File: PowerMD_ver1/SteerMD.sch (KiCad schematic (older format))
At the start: 228 parts, among them P1 SWD, P10 OUT_1, P11 ENC_0, P13 ENC_1, P14 I/O_1, P15 OUT_0, P2 MOTOR_COOLING, P3 CAN, P4 CAN, P5 SERIAL, P6 I/O_0, P7 FAN, P8 BATT_IN, P9 BATT_IN, Q1 MOSFET_N, Q2 MOSFET_N, Q3 MOSFET_N, Q4 MOSFET_N, Q5 MOSFET_N, Q6 MOSFET_N, Q7 MOSFET_N, Q8 MOSFET_N, SW1 RST, SW3 SW0, SW4 SW1, U1 MAX3051, U10 ACS758, U11 POWER_ON, U12 SI8274, U13 ACS758, U14 SI8274, U15 AZ1086H, U16 LOGO, U17 AQM0802, U18 LTC2644, U19 ADRESS, U2 BD9G101, U3 STM32F405RG, U4 SI8274, U5 SI8900, U6 ADC_~RST, U7 BD9G101G, U8 SI8274, U9 BD33FA1, Y1 8MHz

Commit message: だいぶ良いところまで進んだ
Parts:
- added C66, C67: 0.1u, Mizz_lib:1608_WP, symbol SteerMD-rescue:C-Device-MD_Enbarr_x2-rescue-F4_CAN_DCMD-rescue
- C65: footprint Capacitor_SMD:C_0603_1608Metric -> Mizz_lib:1608_WP
- D1, D10, D11, D12, D13, D14, D17, D19, D2, D20, D3, D6: footprint Mizz_lib:1608_WP -> Diode_SMD:D_SOD-123
- R19, R20, R28, R29, R55, R56, R58, R59: value 1 -> 10
- R40: value 4.7k -> 20k
- R75, R76, R77, R78: footprint Resistor_SMD:R_0603_1608Metric -> Mizz_lib:1608_WP
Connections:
- net GNDPWR: now also C66.2, C67.2
- net MOTOR0_OUT: now also C67.1
- net MOTOR1_OUT: now also C66.1
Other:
- moved on the sheet: D12, D17, R77, R78
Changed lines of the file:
@@
 P 8850 3625
 F 0 "R40" H 8920 3671 50  0000 L CNN
-F 1 "4.7k" H 8920 3580 50  0000 L CNN
+F 1 "20k" H 8920 3580 50  0000 L CNN
 F 2 "Resistor_SMD:R_0603_1608Metric" V 8780 3625 50  0001 C CNN
 F 3 "~" H 8850 3625 50  0001 C CNN
@@
 P 13425 8600
 F 0 "R59" V 13218 8600 50  0000 C CNN
-F 1 "1" V 13309 8600 50  0000 C CNN
+F 1 "10" V 13309 8600 50  0000 C CNN
 F 2 "Mizz_lib:1608_WP" V 13355 8600 50  0001 C CNN
 F 3 "~" H 13425 8600 50  0001 C CNN
@@
 F 0 "D11" H 13775 8408 40  0000 C CNN
 F 1 "DIODE" H 13775 8484 40  0000 C CNN
-F 2 "Mizz_lib:1608_WP" H 13775 8600 60  0001 C CNN
+F 2 "Diode_SMD:D_SOD-123" H 13775 8600 60  0001 C CNN
 F 3 "" H 13775 8600 60  0000 C CNN
 	1    13775 8600
@@
 P 13425 7850
 F 0 "R58" V 13218 7850 50  0000 C CNN
-F 1 "1" V 13309 7850 50  0000 C CNN
+F 1 "10" V 13309 7850 50  0000 C CNN
 F 2 "Mizz_lib:1608_WP" V 13355 7850 50  0001 C CNN
 F 3 "~" H 13425 7850 50  0001 C CNN
@@
 F 0 "D3" H 13775 7658 40  0000 C CNN
 F 1 "DIODE" H 13775 7734 40  0000 C CNN
-F 2 "Mizz_lib:1608_WP" H 13775 7850 60  0001 C CNN
+F 2 "Diode_SMD:D_SOD-123" H 13775 7850 60  0001 C CNN
 F 3 "" H 13775 7850 60  0000 C CNN
 	1    13775 7850
@@
 P 11475 8600
 F 0 "R56" V 11268 8600 50  0000 C CNN
-F 1 "1" V 11359 8600 50  0000 C CNN
+F 1 "10" V 11359 8600 50  0000 C CNN
 F 2 "Mizz_lib:1608_WP" V 11405 8600 50  0001 C CNN
 F 3 "~" H 11475 8600 50  0001 C CNN
@@
 F 0 "D2" H 11125 8408 40  0000 C CNN
 F 1 "DIODE" H 11125 8484 40  0000 C CNN
-F 2 "Mizz_lib:1608_WP" H 11125 8600 60  0001 C CNN
+F 2 "Diode_SMD:D_SOD-123" H 11125 8600 60  0001 C CNN
 F 3 "" H 11125 8600 60  0000 C CNN
 	1    11125 8600
@@
 P 11475 7850
 F 0 "R55" V 11268 7850 50  0000 C CNN
-F 1 "1" V 11359 7850 50  0000 C CNN
+F 1 "10" V 11359 7850 50  0000 C CNN
 F 2 "Mizz_lib:1608_WP" V 11405 7850 50  0001 C CNN
 F 3 "~" H 11475 7850 50  0001 C CNN
@@
 F 0 "D1" H 11125 7658 40  0000 C CNN
 F 1 "DIODE" H 11125 7734 40  0000 C CNN
-F 2 "Mizz_lib:1608_WP" H 11125 7850 60  0001 C CNN
+F 2 "Diode_SMD:D_SOD-123" H 11125 7850 60  0001 C CNN
 F 3 "" H 11125 7850 60  0000 C CNN
 	1    11125 7850
@@
 P 13425 5775
 F 0 "R29" V 13218 5775 50  0000 C CNN
-F 1 "1" V 13309 5775 50  0000 C CNN
+F 1 "10" V 13309 5775 50  0000 C CNN
 F 2 "Mizz_lib:1608_WP" V 13355 5775 50  0001 C CNN
 F 3 "~" H 13425 5775 50  0001 C CNN
@@
 F 0 "D20" H 13775 5583 40  0000 C CNN
 F 1 "DIODE" H 13775 5659 40  0000 C CNN
-F 2 "Mizz_lib:1608_WP" H 13775 5775 60  0001 C CNN
+F 2 "Diode_SMD:D_SOD-123" H 13775 5775 60  0001 C CNN
 F 3 "" H 13775 5775 60  0000 C CNN
 	1    13775 5775
@@
 P 13425 5025
 F 0 "R28" V 13218 5025 50  0000 C CNN
-F 1 "1" V 13309 5025 50  0000 C CNN
+F 1 "10" V 13309 5025 50  0000 C CNN
 F 2 "Mizz_lib:1608_WP" V 13355 5025 50  0001 C CNN
 F 3 "~" H 13425 5025 50  0001 C CNN
@@
 F 0 "D19" H 13775 4833 40  0000 C CNN
 F 1 "DIODE" H 13775 4909 40  0000 C CNN
-F 2 "Mizz_lib:1608_WP" H 13775 5025 60  0001 C CNN
+F 2 "Diode_SMD:D_SOD-123" H 13775 5025 60  0001 C CNN
 F 3 "" H 13775 5025 60  0000 C CNN
 	1    13775 5025
@@
 P 11475 5775
 F 0 "R20" V 11268 5775 50  0000 C CNN
-F 1 "1" V 11359 5775 50  0000 C CNN
+F 1 "10" V 11359 5775 50  0000 C CNN
 F 2 "Mizz_lib:1608_WP" V 11405 5775 50  0001 C CNN
 F 3 "~" H 11475 5775 50  0001 C CNN
@@
 F 0 "D14" H 11125 5583 40  0000 C CNN
 F 1 "DIODE" H 11125 5659 40  0000 C CNN
-F 2 "Mizz_lib:1608_WP" H 11125 5775 60  0001 C CNN
+F 2 "Diode_SMD:D_SOD-123" H 11125 5775 60  0001 C CNN
 F 3 "" H 11125 5775 60  0000 C CNN
 	1    11125 5775
@@
 P 11475 5025
 F 0 "R19" V 11268 5025 50  0000 C CNN
-F 1 "1" V 11359 5025 50  0000 C CNN
+F 1 "10" V 11359 5025 50  0000 C CNN
 F 2 "Mizz_lib:1608_WP" V 11405 5025 50  0001 C CNN
 F 3 "~" H 11475 5025 50  0001 C CNN
@@
 F 0 "D13" H 11125 4833 40  0000 C CNN
 F 1 "DIODE" H 11125 4909 40  0000 C CNN
-F 2 "Mizz_lib:1608_WP" H 11125 5025 60  0001 C CNN
+F 2 "Diode_SMD:D_SOD-123" H 11125 5025 60  0001 C CNN
 F 3 "" H 11125 5025 60  0000 C CNN
 	1    11125 5025
@@
 	1    0    0    -1
 $EndComp
-Text Label 14600 3375 0    50   ~ 0
+Text Label 14750 3375 0    50   ~ 0
 OUT0_L
-Text Label 14600 3475 0    50   ~ 0
+Text Label 14750 3475 0    50   ~ 0
 OUT0_R
 $Comp
 L SteerMD-rescue:DIODE-device-MD_Enbarr_x2-rescue-F4_CAN_DCMD-rescue D17
 U 1 1 5E77099F
-P 14400 3475
-F 0 "D17" H 14400 3283 40  0000 C CNN
-F 1 "DIODE" H 14400 3359 40  0000 C CNN
-F 2 "Mizz_lib:1608_WP" H 14400 3475 60  0001 C CNN
-F 3 "" H 14400 3475 60  0000 C CNN
-	1    14400 3475
+P 14550 3475
+F 0 "D17" H 14550 3283 40  0000 C CNN
+F 1 "DIODE" H 14550 3359 40  0000 C CNN
+F 2 "Diode_SMD:D_SOD-123" H 14550 3475 60  0001 C CNN
+F 3 "" H 14550 3475 60  0000 C CNN
+	1    14550 3475
 	-1   0    0    1
 $EndComp
@@
 L SteerMD-rescue:DIODE-device-MD_Enbarr_x2-rescue-F4_CAN_DCMD-rescue D12
 U 1 1 5E771A60
-P 14400 3375
-F 0 "D12" H 14400 3183 40  0000 C CNN
-F 1 "DIODE" H 14400 3259 40  0000 C CNN
-F 2 "Mizz_lib:1608_WP" H 14400 3375 60  0001 C CNN
-F 3 "" H 14400 3375 60  0000 C CNN
-	1    14400 3375
+P 14550 3375
+F 0 "D12" H 14550 3183 40  0000 C CNN
+F 1 "DIODE" H 14550 3259 40  0000 C CNN
+F 2 "Diode_SMD:D_SOD-123" H 14550 3375 60  0001 C CNN
+F 3 "" H 14550 3375 60  0000 C CNN
+	1    14550 3375
 	-1   0    0    1
 $EndComp
 Wire Wire Line
-	14200 3375 14200 3475
+	14350 3375 14350 3475
 $Comp
 L SteerMD-rescue:R-Device-MD_Enbarr_x2-rescue-F4_CAN_DCMD-rescue R77
 U 1 1 5E7BD65D
-P 14200 3625
-F 0 "R77" H 14270 3671 50  0000 L CNN
-F 1 "10k" H 14270 3580 50  0000 L CNN
-F 2 "Resistor_SMD:R_0603_1608Metric" V 14130 3625 50  0001 C CNN
-F 3 "~" H 14200 3625 50  0001 C CNN
-	1    14200 3625
+P 14350 3625
+F 0 "R77" H 14420 3671 50  0000 L CNN
+F 1 "10k" H 14420 3580 50  0000 L CNN
+F 2 "Mizz_lib:1608_WP" V 14280 3625 50  0001 C CNN
+F 3 "~" H 14350 3625 50  0001 C CNN
+	1    14350 3625
 	1    0    0    -1
 $EndComp
-Connection ~ 14200 3475
+Connection ~ 14350 3475
 $Comp
 L SteerMD-rescue:R-Device-MD_Enbarr_x2-rescue-F4_CAN_DCMD-rescue R78
 U 1 1 5E7BED02
-P 14200 3975
-F 0 "R78" H 14270 4021 50  0000 L CNN
-F 1 "1k" H 14270 3930 50  0000 L CNN
-F 2 "Resistor_SMD:R_0603_1608Metric" V 14130 3975 50  0001 C CNN
-F 3 "~" H 14200 3975 50  0001 C CNN
-	1    14200 3975
+P 14350 3975
+F 0 "R78" H 14420 4021 50  0000 L CNN
+F 1 "1k" H 14420 3930 50  0000 L CNN
+F 2 "Mizz_lib:1608_WP" V 14280 3975 50  0001 C CNN
+F 3 "~" H 14350 3975 50  0001 C CNN
+	1    14350 3975
 	1    0    0    -1
 $EndComp
-Text Label 14150 3800 2    50   ~ 0
+Text Label 14300 3800 2    50   ~ 0
 MOTOR0_OUT
 Wire Wire Line
-	14150 3800 14200 3800
+	14300 3800 14350 3800
 Wire Wire Line
-	14200 3800 14200 3775
+	14350 3800 14350 3775
 Wire Wire Line
-	14200 3800 14200 3825
-Connection ~ 14200 3800
+	14350 3800 14350 3825
+Connection ~ 14350 3800
 $Comp
 L SteerMD-rescue:GNDPWR-power-MD_Enbarr_x2-rescue-F4_CAN_DCMD-rescue #PWR0173
 U 1 1 5E829E9C
-P 14200 4125
-F 0 "#PWR0173" H 14200 3925 50  0001 C CNN
-F 1 "GNDPWR" H 14204 3971 50  0000 C CNN
-F 2 "" H 14200 4075 50  0001 C CNN
-F 3 "" H 14200 4075 50  0001 C CNN
-	1    14200 4125
+P 14350 4125
+F 0 "#PWR0173" H 14350 3925 50  0001 C CNN
+F 1 "GNDPWR" H 14354 3971 50  0000 C CNN
+F 2 "" H 14350 4075 50  0001 C CNN
+F 3 "" H 14350 4075 50  0001 C CNN
+	1    14350 4125
 	1    0    0    -1
 $EndComp
@@
 F 0 "D10" H 13625 3283 40  0000 C CNN
 F 1 "DIODE" H 13625 3359 40  0000 C CNN
-F 2 "Mizz_lib:1608_WP" H 13625 3475 60  0001 C CNN
+F 2 "Diode_SMD:D_SOD-123" H 13625 3475 60  0001 C CNN
 F 3 "" H 13625 3475 60  0000 C CNN
 	1    13625 3475
@@
 F 0 "D6" H 13625 3183 40  0000 C CNN
 F 1 "DIODE" H 13625 3259 40  0000 C CNN
-F 2 "Mizz_lib:1608_WP" H 13625 3375 60  0001 C CNN
+F 2 "Diode_SMD:D_SOD-123" H 13625 3375 60  0001 C CNN
 F 3 "" H 13625 3375 60  0000 C CNN
 	1    13625 3375
@@
 F 0 "R75" H 13495 3671 50  0000 L CNN
 F 1 "10k" H 13495 3580 50  0000 L CNN
-F 2 "Resistor_SMD:R_0603_1608Metric" V 13355 3625 50  0001 C CNN
+F 2 "Mizz_lib:1608_WP" V 13355 3625 50  0001 C CNN
 F 3 "~" H 13425 3625 50  0001 C CNN
 	1    13425 3625
@@
 F 0 "R76" H 13495 4021 50  0000 L CNN
 F 1 "1k" H 13495 3930 50  0000 L CNN
-F 2 "Resistor_SMD:R_0603_1608Metric" V 13355 3975 50  0001 C CNN
+F 2 "Mizz_lib:1608_WP" V 13355 3975 50  0001 C CNN
 F 3 "~" H 13425 3975 50  0001 C CNN
 	1    13425 3975
@@
 F 0 "C65" V 12023 3650 50  0000 C CNN
 F 1 "0.1u" V 12114 3650 50  0000 C CNN
-F 2 "Capacitor_SMD:C_0603_1608Metric" H 12313 3500 50  0001 C CNN
+F 2 "Mizz_lib:1608_WP" H 12313 3500 50  0001 C CNN
 F 3 "~" H 12275 3650 50  0001 C CNN
 	1    12275 3650
@@
 Text Label 9125 2425 0    50   ~ 0
 MOTOR1_VOLTAGE_DAC
+$Comp
+L SteerMD-rescue:C-Device-MD_Enbarr_x2-rescue-F4_CAN_DCMD-rescue C67
+U 1 1 5E5CD9E6
+P 14675 3975
+F 0 "C67" H 14790 4021 50  0000 L CNN
+F 1 "0.1u" H 14790 3930 50  0000 L CNN
+F 2 "Mizz_lib:1608_WP" H 14713 3825 50  0001 C CNN
+F 3 "~" H 14675 3975 50  0001 C CNN
+	1    14675 3975
+	1    0    0    -1
+$EndComp
+Wire Wire Line
+	14675 4125 14350 4125
+Connection ~ 14350 4125
+Wire Wire Line
+	14350 3800 14675 3800
+Wire Wire Line
+	14675 3800 14675 3825
+$Comp
+L SteerMD-rescue:C-Device-MD_Enbarr_x2-rescue-F4_CAN_DCMD-rescue C66
+U 1 1 5E64485E
+P 13750 3975
+F 0 "C66" H 13865 4021 50  0000 L CNN
+F 1 "0.1u" H 13865 3930 50  0000 L CNN
+F 2 "Mizz_lib:1608_WP" H 13788 3825 50  0001 C CNN
+F 3 "~" H 13750 3975 50  0001 C CNN
+	1    13750 3975
+	1    0    0    -1
+$EndComp
+Wire Wire Line
+	13750 3825 13750 3800
+Wire Wire Line
+	13750 3800 13425 3800
+Wire Wire Line
+	13750 4125 13425 4125
+Connection ~ 13425 4125
 $EndSCHEMATC

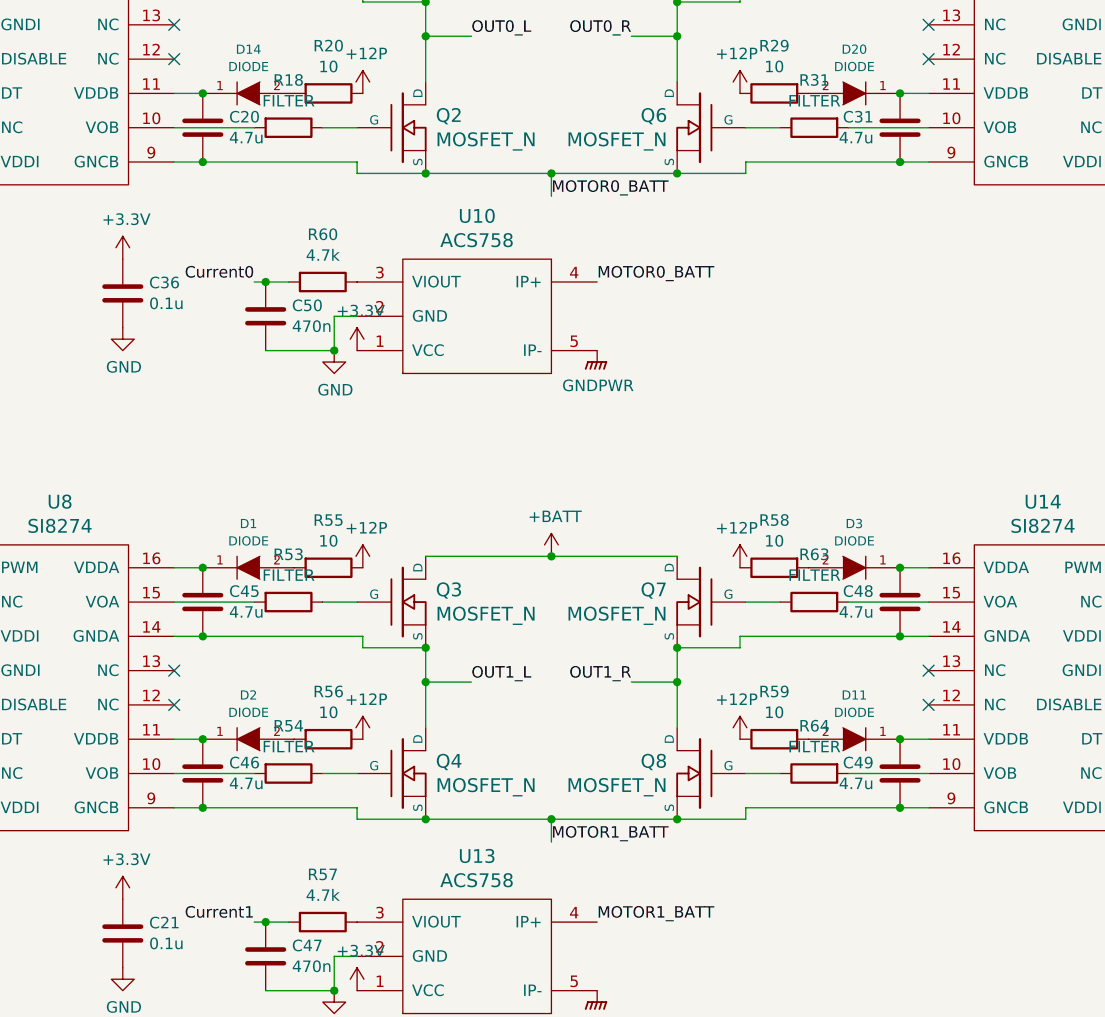
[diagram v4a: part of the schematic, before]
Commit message: ローサイドセンシングバージョンのMDも一応できた
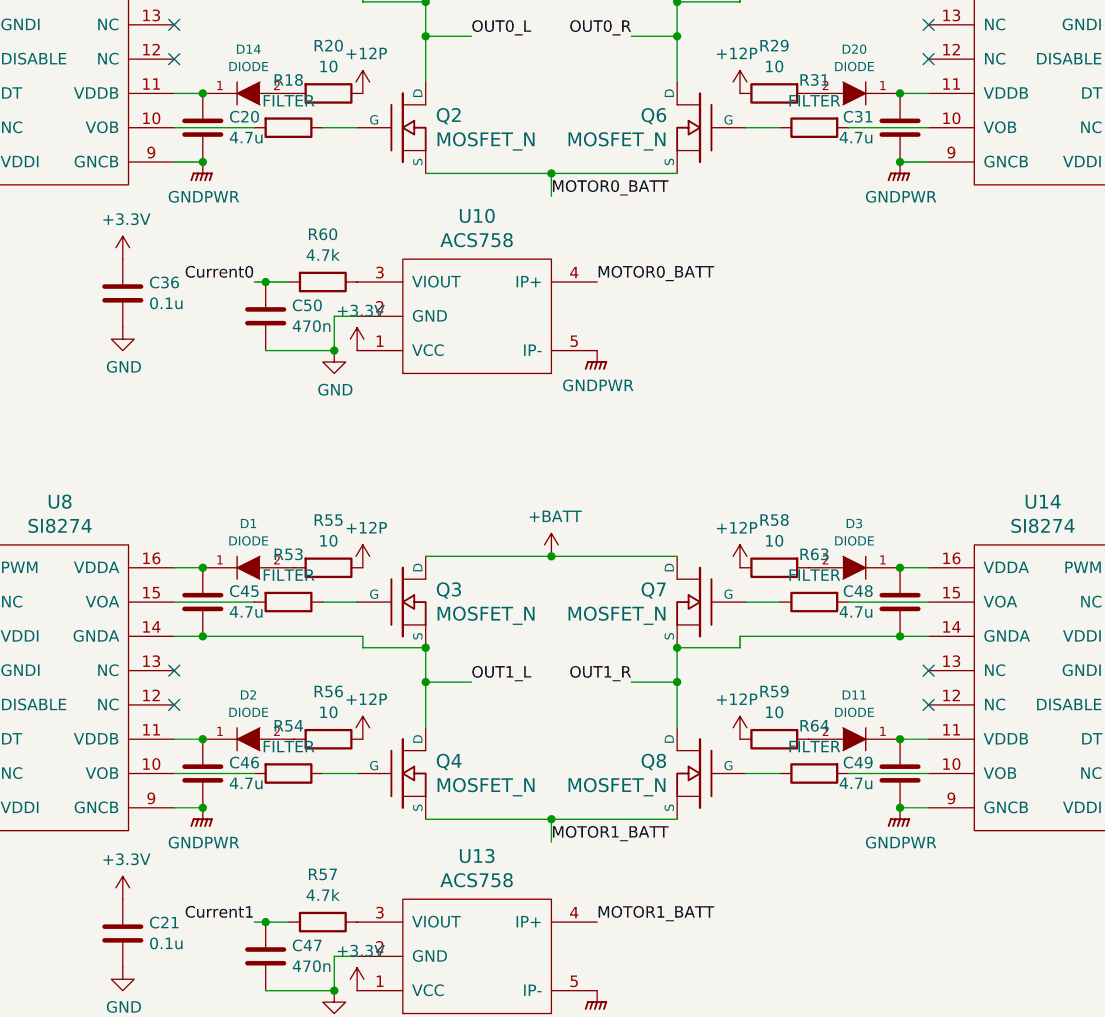
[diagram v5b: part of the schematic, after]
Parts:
- R34: footprint Resistor_SMD:R_0603_1608Metric -> Mizz_lib:1608_WP
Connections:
- net GNDPWR: now also C20.2, C31.2, C46.2, C49.2, U12.9 (GNCB), U14.9 (GNCB), U4.9 (GNCB), U8.9 (GNCB)
- net MOTOR0_BATT: no longer C20.2, C31.2, U12.9 (GNCB), U4.9 (GNCB)
- net MOTOR1_BATT: no longer C46.2, C49.2, U14.9 (GNCB), U8.9 (GNCB)
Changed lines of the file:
@@
 F 0 "R34" V 14193 2000 50  0000 C CNN
 F 1 "510" V 14284 2000 50  0000 C CNN
-F 2 "Resistor_SMD:R_0603_1608Metric" V 14330 2000 50  0001 C CNN
+F 2 "Mizz_lib:1608_WP" V 14330 2000 50  0001 C CNN
 F 3 "~" H 14400 2000 50  0001 C CNN
 	1    14400 2000
@@
 Wire Wire Line
 	14100 8150 13975 8150
-Connection ~ 13975 8900
-Connection ~ 13000 8950
-Wire Wire Line
-	13300 8900 13975 8900
-Wire Wire Line
-	13300 8950 13300 8900
-Wire Wire Line
-	13000 8950 13300 8950
 Wire Wire Line
 	14100 8900 13975 8900
@@
 	-1   0    0    -1
 $EndComp
-Connection ~ 11900 8950
 $Comp
 L SteerMD-rescue:MOSFET_N-Miz-F4_CAN_DCMD-rescue Q8
@@
 	1    0    0    -1
 $EndComp
-Wire Wire Line
-	10925 8900 11600 8900
-Connection ~ 10925 8900
-Wire Wire Line
-	11600 8950 11900 8950
-Wire Wire Line
-	11600 8900 11600 8950
 Wire Wire Line
 	10800 8900 10925 8900
@@
 Wire Wire Line
 	14100 5325 13975 5325
-Connection ~ 13975 6075
-Connection ~ 13000 6125
-Wire Wire Line
-	13300 6075 13975 6075
-Wire Wire Line
-	13300 6125 13300 6075
-Wire Wire Line
-	13000 6125 13300 6125
 Wire Wire Line
 	14100 6075 13975 6075
@@
 	12450 6125 13000 6125
 Connection ~ 12450 6125
-Connection ~ 11900 6125
 Wire Wire Line
 	11900 6125 12450 6125
@@
 	1    0    0    -1
 $EndComp
-Wire Wire Line
-	10925 6075 11600 6075
-Connection ~ 10925 6075
-Wire Wire Line
-	11600 6125 11900 6125
-Wire Wire Line
-	11600 6075 11600 6125
 Wire Wire Line
 	10800 6075 10925 6075
@@
 	13750 4125 13425 4125
 Connection ~ 13425 4125
+$Comp
+L SteerMD-rescue:GNDPWR-power-MD_Enbarr_x2-rescue-F4_CAN_DCMD-rescue #PWR?
+U 1 1 5E53267A
+P 10925 6075
+F 0 "#PWR?" H 10925 5875 50  0001 C CNN
+F 1 "GNDPWR" H 10929 5921 50  0000 C CNN
+F 2 "" H 10925 6025 50  0001 C CNN
+F 3 "" H 10925 6025 50  0001 C CNN
+	1    10925 6075
+	1    0    0    -1
+$EndComp
+Connection ~ 10925 6075
+$Comp
+L SteerMD-rescue:GNDPWR-power-MD_Enbarr_x2-rescue-F4_CAN_DCMD-rescue #PWR?
+U 1 1 5E536DEE
+P 13975 6075
+F 0 "#PWR?" H 13975 5875 50  0001 C CNN
+F 1 "GNDPWR" H 13979 5921 50  0000 C CNN
+F 2 "" H 13975 6025 50  0001 C CNN
+F 3 "" H 13975 6025 50  0001 C CNN
+	1    13975 6075
+	1    0    0    -1
+$EndComp
+Connection ~ 13975 6075
+$Comp
+L SteerMD-rescue:GNDPWR-power-MD_Enbarr_x2-rescue-F4_CAN_DCMD-rescue #PWR?
+U 1 1 5E53E4B4
+P 10925 8900
+F 0 "#PWR?" H 10925 8700 50  0001 C CNN
+F 1 "GNDPWR" H 10929 8746 50  0000 C CNN
+F 2 "" H 10925 8850 50  0001 C CNN
+F 3 "" H 10925 8850 50  0001 C CNN
+	1    10925 8900
+	1    0    0    -1
+$EndComp
+Connection ~ 10925 8900
+$Comp
+L SteerMD-rescue:GNDPWR-power-MD_Enbarr_x2-rescue-F4_CAN_DCMD-rescue #PWR?
+U 1 1 5E53EA94
+P 13975 8900
+F 0 "#PWR?" H 13975 8700 50  0001 C CNN
+F 1 "GNDPWR" H 13979 8746 50  0000 C CNN
+F 2 "" H 13975 8850 50  0001 C CNN
+F 3 "" H 13975 8850 50  0001 C CNN
+	1    13975 8900
+	1    0    0    -1
+$EndComp
+Connection ~ 13975 8900
 $EndSCHEMATC

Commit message: 電流制御MD(仮)配線(仮)完成(仮)
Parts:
- R37: value 50k -> 3.9k
- R38: value 10k -> 680
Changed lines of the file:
@@
 P 3275 1450
 F 0 "R37" H 3345 1496 50  0000 L CNN
-F 1 "50k" H 3345 1405 50  0000 L CNN
+F 1 "3.9k" H 3345 1405 50  0000 L CNN
 F 2 "Resistor_SMD:R_0603_1608Metric" V 3205 1450 50  0001 C CNN
 F 3 "~" H 3275 1450 50  0001 C CNN
@@
 P 3275 1800
 F 0 "R38" H 3345 1846 50  0000 L CNN
-F 1 "10k" H 3345 1755 50  0000 L CNN
+F 1 "680" H 3345 1755 50  0000 L CNN
 F 2 "Resistor_SMD:R_0603_1608Metric" V 3205 1800 50  0001 C CNN
 F 3 "~" H 3275 1800 50  0001 C CNN

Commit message: 上げ忘れていた工大祭モータドライバ(前身開発基板)とJetsonNanoの電源基板関係
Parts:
- U18: symbol Miz:LTC2644 -> SteerMD-rescue:LTC2644-Miz
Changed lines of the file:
@@
 	12450 6225 12450 6125
 $Comp
-L Miz:LTC2644 U18
+L SteerMD-rescue:LTC2644-Miz U18
 U 1 1 5E609A08
 P 11675 3750
